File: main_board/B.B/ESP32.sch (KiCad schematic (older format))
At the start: 37 parts, among them J5 USB_C_Receptacle_USB2.0, Q3 CJ3134K, Q4 Q_NPN_BCE, Q5 Q_NPN_BCE, SW1 SW_DIP_x01, SW2 SW_DIP_x01, U64 CP2102N-A01-GQFN28, U65 ESP32-WROVER

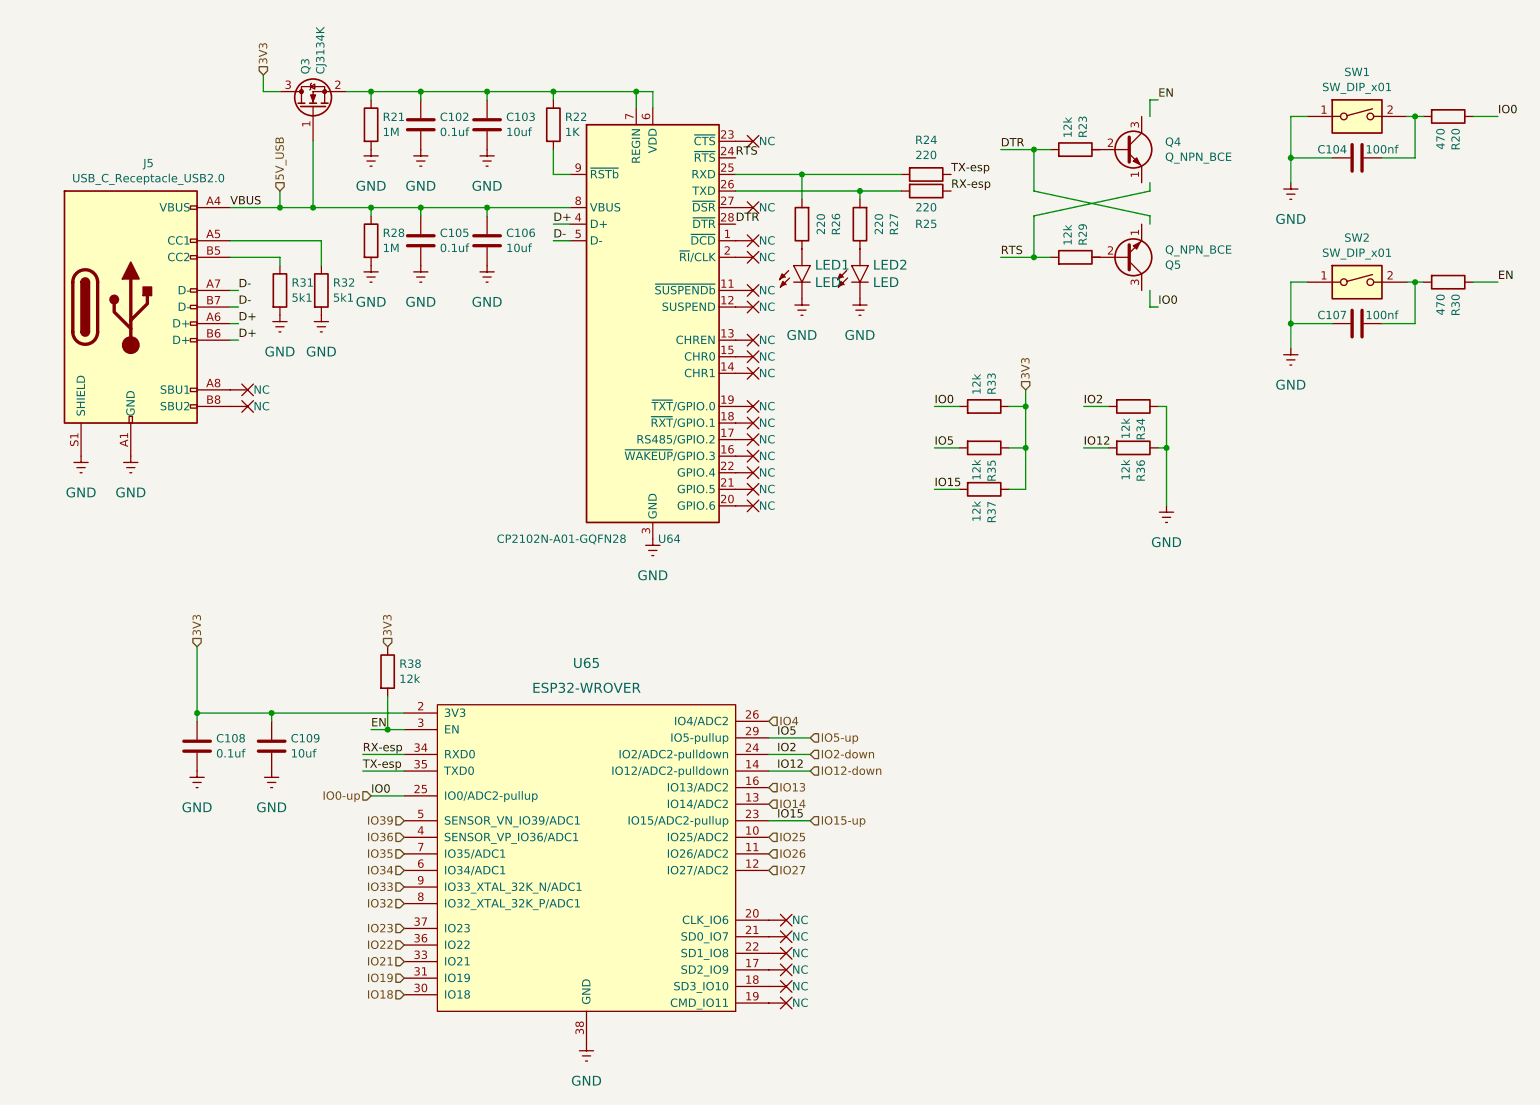
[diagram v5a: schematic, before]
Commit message: orezavani
smazaní A9G, SD karty, a zvuku
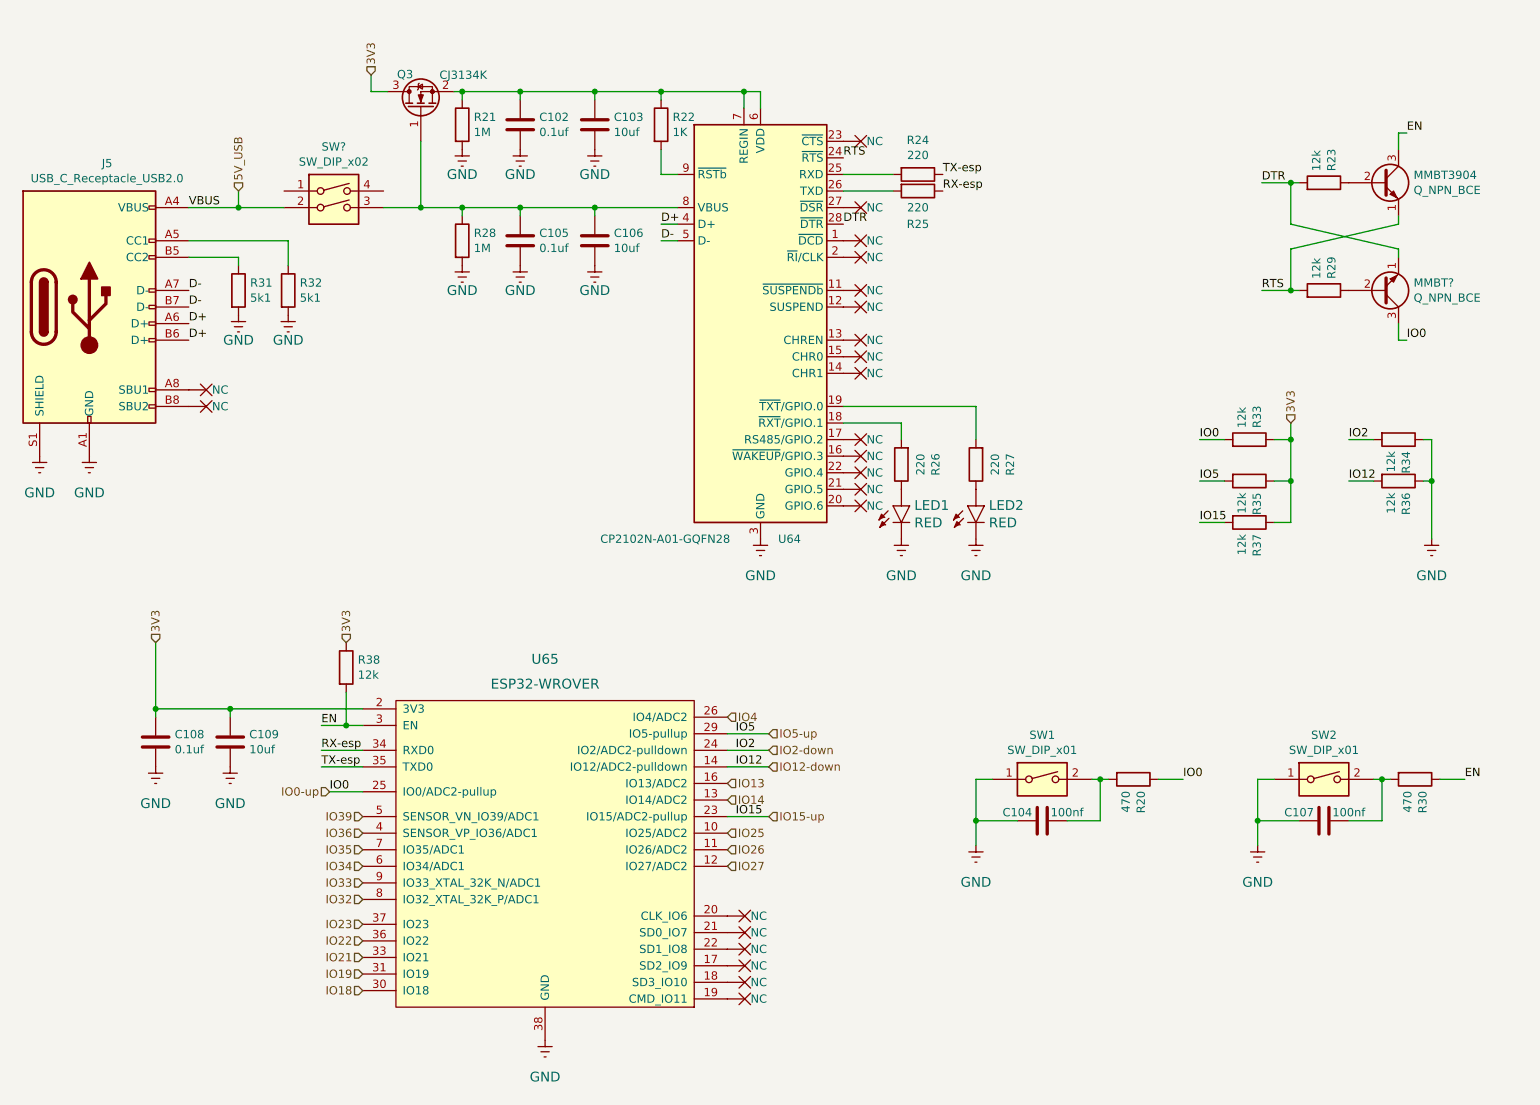
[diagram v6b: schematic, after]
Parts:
- removed Q4, Q5: Q_NPN_BCE, Package_TO_SOT_SMD:SOT-23, symbol Device:Q_NPN_BCE
- added MMBT3904, MMBT?: Q_NPN_BCE, Package_TO_SOT_SMD:SOT-23, symbol B.B-rescue:Q_NPN_BCE
- added SW?: SW_DIP_x02, symbol Switch:SW_DIP_x02
- LED1, LED2: value LED -> RED
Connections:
- wire segments 105 -> 102
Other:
- moved on the sheet: C102, C103, C104, C105, C106, C107, C108, C109, J5, LED1, LED2, Q3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

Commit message: nabijecka
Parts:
- Q3: value CJ3134K -> AO3400A; LCSC C110100 -> C20917
- gave numbers to parts that had none: 2
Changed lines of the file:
@@
 $Descr A4 11693 8268
 encoding utf-8
-Sheet 6 7
+Sheet 8 8
 Title ""
 Date ""
@@
 P 3900 1350
 F 0 "Q3" V 4104 1396 50  0000 L CNN
-F 1 "CJ3134K" V 4100 950 50  0000 L CNN
+F 1 "AO3400A" V 4100 950 50  0000 L CNN
 F 2 "Package_TO_SOT_SMD:SOT-23" H 4100 1275 50  0001 L CIN
 F 3 "https://datasheet.lcsc.com/szlcsc/Changjiang-Electronics-Tech-CJ-CJ3134K_C110100.pdf" H 3900 1350 50  0001 L CNN
-F 4 "C110100" H 3900 1350 50  0001 C CNN "LCSC"
+F 4 "C20917" H 3900 1350 50  0001 C CNN "LCSC"
 	1    3900 1350
 	0    -1   -1   0
@@
 $EndComp
 $Comp
-L B.B-rescue:Q_NPN_BCE MMBT?
+L B.B-rescue:Q_NPN_BCE MMBT1
 U 1 1 60279667
 P 9750 2450
-F 0 "MMBT?" H 9891 2404 50  0000 L CNN
+F 0 "MMBT1" H 9891 2404 50  0000 L CNN
 F 1 "Q_NPN_BCE" H 9891 2495 50  0000 L CNN
 F 2 "Package_TO_SOT_SMD:SOT-23" H 9900 2550 50  0001 C CNN
@@
 $EndComp
 $Comp
-L Switch:SW_DIP_x02 SW?
+L Switch:SW_DIP_x02 SW4
 U 1 1 5FB55D9C
 P 3375 1950
-F 0 "SW?" H 3375 2317 50  0000 C CNN
+F 0 "SW4" H 3375 2317 50  0000 C CNN
 F 1 "SW_DIP_x02" H 3375 2226 50  0000 C CNN
 F 2 "" H 3375 1950 50  0001 C CNN

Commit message: odpojovan_nabijecky
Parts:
- added R?: 220, Resistor_SMD:R_0402_1005Metric, symbol Device:R
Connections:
- net at C102.1, C103.1, Q3.2 (S)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: now also R?.2
- new net cable_connected: R?.1
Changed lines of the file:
@@
 F 1 "AO3400A" V 4100 950 50  0000 L CNN
 F 2 "Package_TO_SOT_SMD:SOT-23" H 4100 1275 50  0001 L CIN
-F 3 "https://datasheet.lcsc.com/szlcsc/Changjiang-Electronics-Tech-CJ-CJ3134K_C110100.pdf" H 3900 1350 50  0001 L CNN
+F 3 "https://datasheet.lcsc.com/szlcsc/Alpha-Omega-Semicon-AOS-AO3400A_C20917.pdf" H 3900 1350 50  0001 L CNN
 F 4 "C20917" H 3900 1350 50  0001 C CNN "LCSC"
 	1    3900 1350
@@
 Wire Wire Line
 	4150 1950 4500 1950
+Text HLabel 6300 1250 2    50   Input ~ 0
+cable_connected
+$Comp
+L Device:R R?
+U 1 1 5FB94C99
+P 6150 1250
+AR Path="/5FA3274C/5FB94C99" Ref="R?"  Part="1"
+AR Path="/5F9EE529/5FB94C99" Ref="R?"  Part="1"
+AR Path="/5F77B818/5FB94C99" Ref="R?"  Part="1"
+F 0 "R?" V 5943 1250 50  0000 C CNN
+F 1 "220" V 6034 1250 50  0000 C CNN
+F 2 "Resistor_SMD:R_0402_1005Metric" V 6080 1250 50  0001 C CNN
+F 3 "~" H 6150 1250 50  0001 C CNN
+F 4 "C25092" V 6150 1250 50  0001 C CNN "LCSC"
+	1    6150 1250
+	0    1    1    0
+$EndComp
+Wire Wire Line
+	6000 1250 5950 1250
+Connection ~ 5950 1250
 $EndSCHEMATC
